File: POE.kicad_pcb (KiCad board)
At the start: 2 copper layers, 40 x 70 mm, 13 parts, among them J1 Conn_01x02_Male

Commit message: Some tweaking and explanation(s)
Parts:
- moved J1 13.0 mm to (114.5, 105.1), turned to 90 degrees
- moved D1 8.25 mm to (88.0, 74.0)
- moved D2 7.75 mm to (88.0, 82.0), turned to 90 degrees
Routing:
- net VA1: track 69.3 -> 48.2 mm
- net VA2: track 65.0 -> 53.3 mm
- net VB2: track 50.9 -> 57.8 mm
- net VB1: track 56.2 -> 59.6 mm
- net Vin+: track 30.2 -> 32.6 mm
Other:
- board text added: "- +"
- board text removed: "x"

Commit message: ...
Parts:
- moved RJ45-1 16.4 mm to (111.0, 125.8), turned to -135 degrees
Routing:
- net VA2: track 53.3 -> 58.0 mm
- net VB2: track 57.8 -> 62.0 mm
- net VB1: track 59.6 -> 63.1 mm
- net VA1: track 48.2 -> 51.1 mm
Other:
- outline, holes or cut-outs redrawn
- board text added: "Wiremold Surface Mount Box internals"
- board text removed: "Wiremold Surface Mount Box internals (likely still need non-strain-releifed Eth cable tho...)"

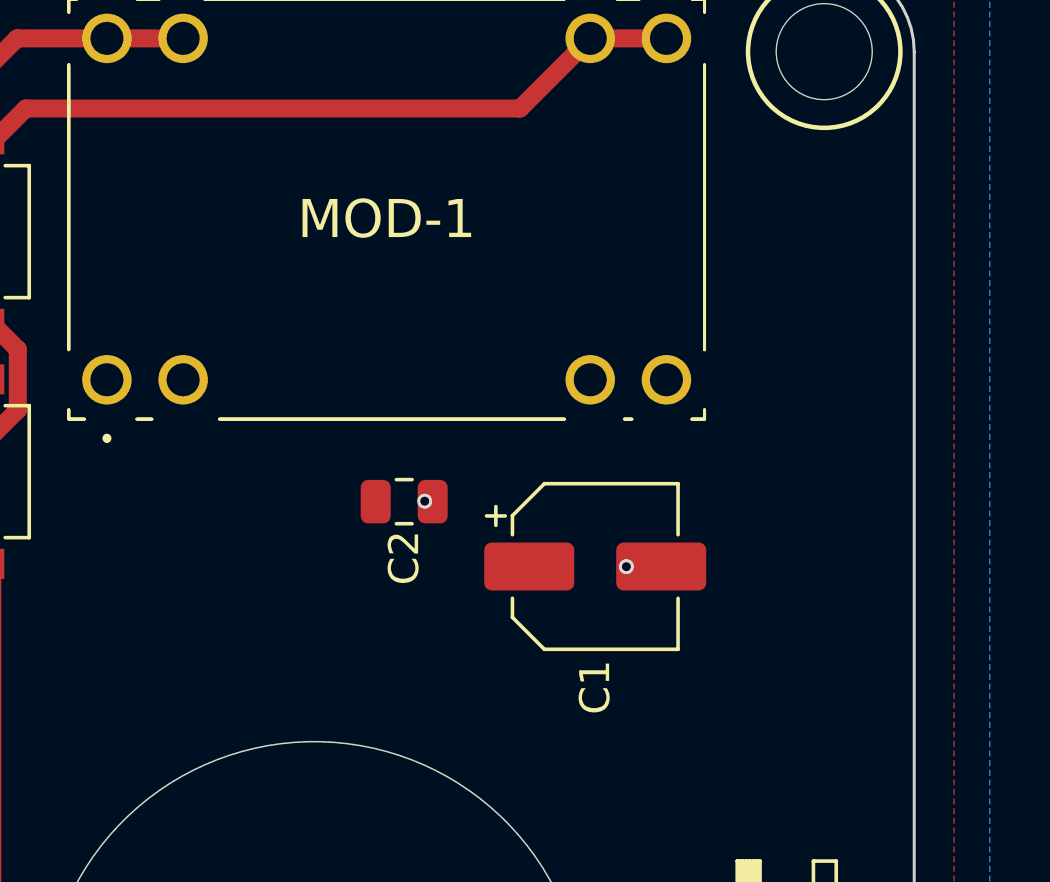
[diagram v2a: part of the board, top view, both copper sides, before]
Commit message: Added adjustment & minLoad resistors
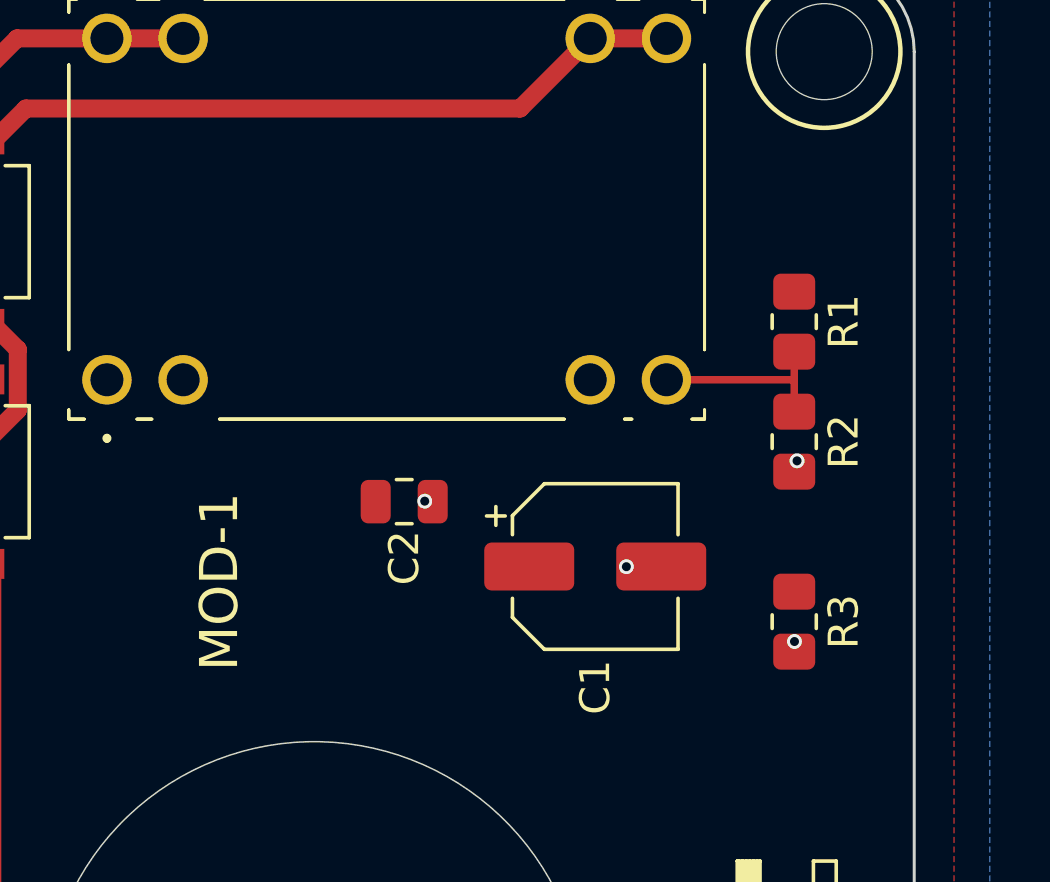
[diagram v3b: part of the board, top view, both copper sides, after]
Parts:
- added R1: ?, Resistor_SMD:R_0805_2012Metric_Pad1.20x1.40mm_HandSolder, F.Cu at (116.0, 77.0)
- added R2: ?, Resistor_SMD:R_0805_2012Metric_Pad1.20x1.40mm_HandSolder, F.Cu at (116.0, 81.0)
- added R3: Rmin, Resistor_SMD:R_0805_2012Metric_Pad1.20x1.40mm_HandSolder, F.Cu at (116.0, 87.0)
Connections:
- MOD-1 pad 4: unconnected-(MOD-1-Pad4) -> ADJ
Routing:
- net ADJ: track 0.00 -> 6.27 mm
- net GND: vias 2 -> 4

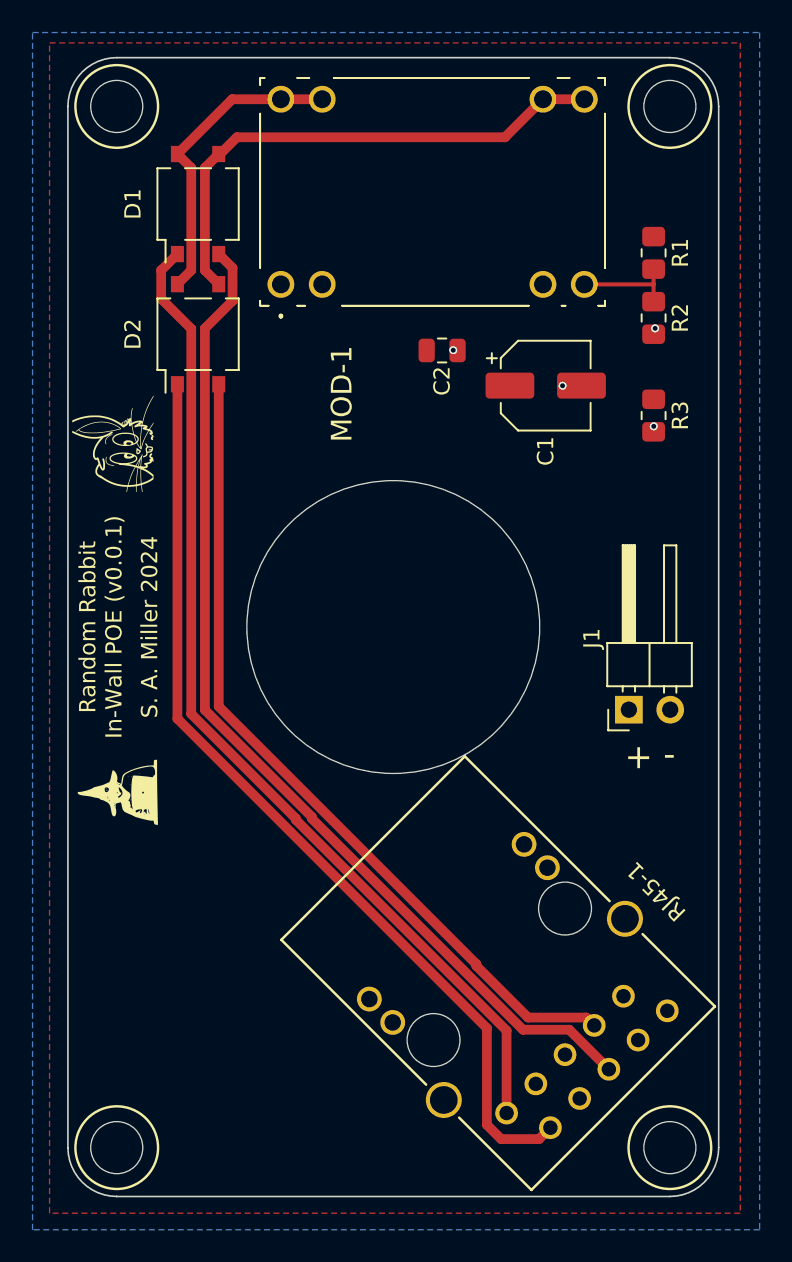
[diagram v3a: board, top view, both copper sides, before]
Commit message: upgraded from the overkill Ethernet jack to a better fit plus magnetics
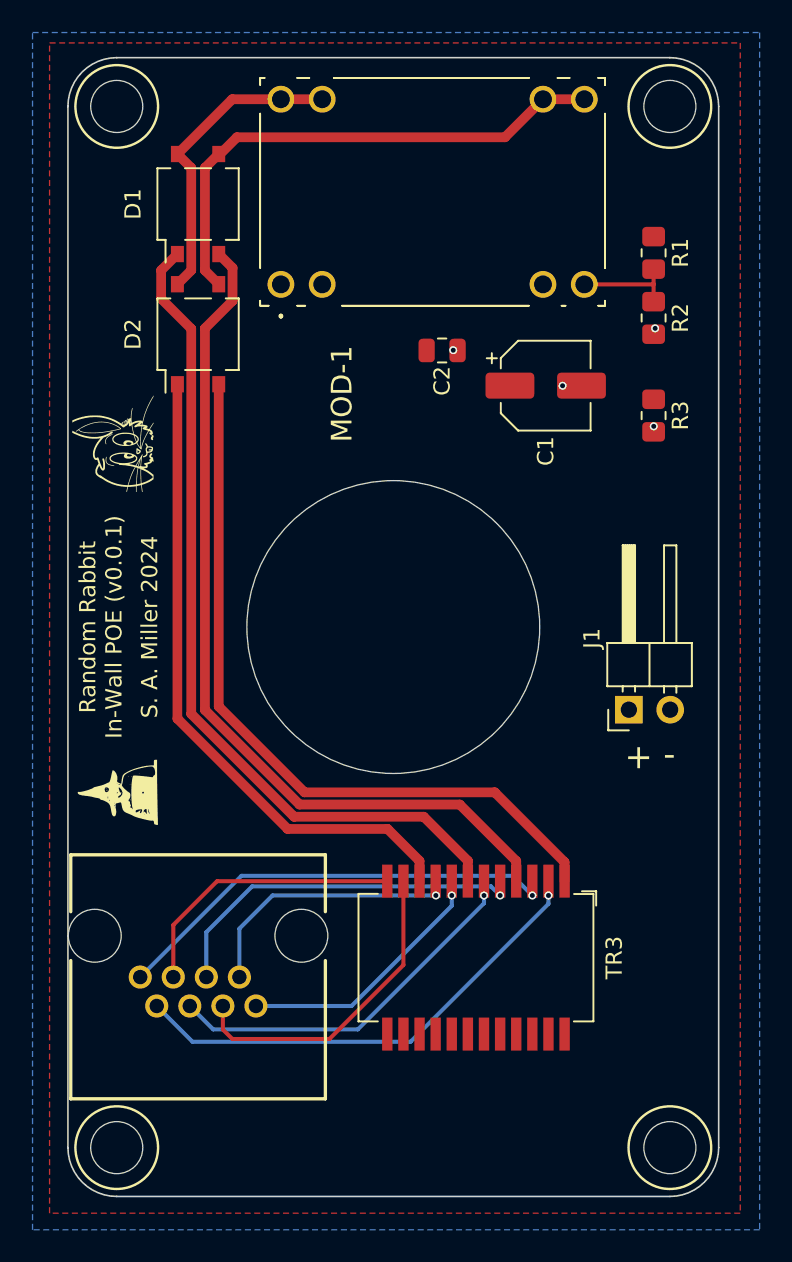
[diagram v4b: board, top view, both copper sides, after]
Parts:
- removed RJ45-1: ARJM11D7114ABEW2, Tinker:CONN_ARJM11D7-114-AB-EW2_ABR
- added RJ1: RC01374, tightstuff:RC01374, F.Cu at (88.0, 121.5)
- added TR3: TG111-MSC13LF, Transformer_SMD:Transformer_Ethernet_HALO_TG111-MSC13, F.Cu at (105.1, 120.3)
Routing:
- net Net-(RJ1-Pad2): track 0.00 -> 29.0 mm, vias 0 -> 1
- net Net-(RJ1-Pad1): track 0.00 -> 27.2 mm, vias 0 -> 1
- net Net-(RJ1-Pad4): track 0.00 -> 22.4 mm, vias 0 -> 1
- net Net-(RJ1-Pad5): track 0.00 -> 22.2 mm, vias 0 -> 1
- net Net-(RJ1-Pad6): track 0.00 -> 19.8 mm
- net VA2: track 58.0 -> 40.3 mm
- net Net-(RJ1-Pad3): track 0.00 -> 17.5 mm
- net Net-(RJ1-Pad7): track 0.00 -> 15.9 mm, vias 0 -> 1
- net Net-(RJ1-Pad8): track 0.00 -> 15.2 mm, vias 0 -> 1
- net VB2: track 62.0 -> 51.4 mm
- net VB1: track 63.1 -> 53.3 mm
- net VA1: track 51.1 -> 46.2 mm
